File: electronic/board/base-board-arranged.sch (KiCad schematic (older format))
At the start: 96 parts, among them P1 BEAGLEBONE_BLACK, P100_0 CONN_02X10, P100_1 CONN_02X10, P100_10 CONN_02X10, P100_11 CONN_02X10, P100_12 CONN_02X10, P100_13 CONN_02X10, P100_14 CONN_02X10, P100_15 CONN_02X10, P100_16 CONN_02X10, P100_17 CONN_02X10, P100_2 CONN_02X10, P100_3 CONN_02X10, P100_4 CONN_02X10, P100_5 CONN_02X10, P100_6 CONN_02X10, P100_7 CONN_02X10, P100_8 CONN_02X10, P100_9 CONN_02X10, P2 I2C, P3 PWR, P5 CONN_02X10, P6 CONN_02X10

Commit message: Some hw, +others
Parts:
- added Q1: IRF540N, TO-220, symbol IRF540N
- added R2: 1k, Resistors_ThroughHole:Resistor_Ceramic_Horizontal_L50mm-W14mm-H13mm-p60mm, symbol R
- R100_16: footprint w_pth_resistors:R25x8 -> Resistors_ThroughHole:Resistor_Ceramic_Horizontal_L50mm-W14mm-H13mm-p60mm
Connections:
- net GND: no longer P1.A1 (GND), P1.A2 (P2), P1.B1 (GND), P1.B2 (P2), P3.2 (P2), P5.1 (P1), P5.2 (P2), P6.1 (P1), P6.2 (P2)
- net GND3: now also Q1.3 (S); no longer B4.2
- net SYS_RESETn: now also R2.2
- new net: B4.2, Q1.2 (D)
- new net: P5.1 (P1), P5.2 (P2)
- new net: Q1.1 (G), R2.1
- new net GND1: P1.B1 (GND), P1.B2 (P2), P3.2 (P2), P6.1 (P1), P6.2 (P2)
- new net GND2: P1.A1 (GND), P1.A2 (P2)
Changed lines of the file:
@@
 EESchema Schematic File Version 2
+LIBS:beagleboard
 LIBS:power
 LIBS:device
@@
 LIBS:contrib
 LIBS:valves
+LIBS:base-board-arranged-cache
 EELAYER 25 0
 EELAYER END
@@
 GPIO2_11
 Text Label 1100 8650 2    60   ~ 0
-GND
+GND2
 Text Label 1900 8650 0    60   ~ 0
-GND
+GND2
 Text Label 3300 8650 2    60   ~ 0
-GND
+GND1
 Text Label 4100 8650 0    60   ~ 0
-GND
+GND1
 Text Label 3300 8750 2    60   ~ 0
 DC_3.3Ve
@@
 	1    0    0    -1
 $EndComp
-Text Label 14450 2900 0    60   ~ 0
+Text Label 14450 4125 3    60   ~ 0
 GND3
 $Comp
@@
 Text Label 1150 5150 2    60   ~ 0
 12V+
-Text Label 1150 4850 2    60   ~ 0
-GND
 Text Label 1150 4950 2    60   ~ 0
 DC_3.3V
@@
 GND
 Text Label 2300 4850 2    60   ~ 0
-GND
+GND1
 Wire Wire Line
 	1150 4850 1650 4850
@@
 F 0 "R100_16" V 2230 5750 50  0000 C CNN
 F 1 "1K" V 2150 5750 50  0000 C CNN
-F 2 "w_pth_resistors:R25x8" V 2080 5750 30  0000 C CNN
+F 2 "Resistors_ThroughHole:Resistor_Ceramic_Horizontal_L50mm-W14mm-H13mm-p60mm" V 2080 5750 30  0000 C CNN
 F 3 "" H 2150 5750 30  0000 C CNN
 	1    2150 5750
@@
 $EndComp
 Text Label 2100 4425 2    60   ~ 0
-GND
+GND1
 Text Label 1550 4325 2    60   ~ 0
 PWR_BUT
@@
 Wire Wire Line
 	1850 4325 2100 4325
+$Comp
+L IRF540N Q1
+U 1 1 57B8B01B
+P 14350 3925
+F 0 "Q1" H 14650 4000 50  0000 L CNN
+F 1 "IRF540N" H 14600 3925 50  0000 L CNN
+F 2 "TO-220" H 14600 3850 50  0000 L CIN
+F 3 "" H 14350 3925 50  0000 L CNN
+	1    14350 3925
+	1    0    0    -1
+$EndComp
+$Comp
+L R R2
+U 1 1 57B8F1D2
+P 13850 3975
+F 0 "R2" V 13930 3975 50  0000 C CNN
+F 1 "1k" V 13850 3975 50  0000 C CNN
+F 2 "Resistors_ThroughHole:Resistor_Ceramic_Horizontal_L50mm-W14mm-H13mm-p60mm" V 13780 3975 30  0000 C CNN
+F 3 "" H 13850 3975 30  0000 C CNN
+	1    13850 3975
+	0    1    1    0
+$EndComp
+Text Label 13700 3975 2    60   ~ 0
+SYS_RESETn
+Wire Wire Line
+	14450 3725 14450 2900
+Wire Wire Line
+	14000 3975 14150 3975
 $EndSCHEMATC

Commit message: Main Board
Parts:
- removed R103_15: 1K, w_pth_resistors:RC03, symbol R
- added R3: 47k, w_pth_resistors:RC03, symbol R
- B3, B4: footprint w_pth_resistors:RC05 -> w_pth_resistors:RC07
- Q1: footprint TO-220 -> Transistors_TO-220:TO-220_Neutral123_Horizontal_LargePads
- R100_10, R100_11, R100_12, R100_13, R100_15, R100_4, R100_5, R100_6, R100_7, R100_9, R101_10, R101_11, R101_12, R101_15, R101_4, R101_5, R101_6, R101_7, R101_9, R102_10, R102_11, R102_12, R102_4, R102_5, R102_6, R102_7, R102_9, R103_10, R103_11, R103_12, R103_4, R103_5, R103_6, R103_7, R103_9: footprint w_pth_resistors:RC03 -> w_pth_resistors:RC07
- R100_16: footprint Resistors_ThroughHole:Resistor_Ceramic_Horizontal_L50mm-W14mm-H13mm-p60mm -> w_pth_resistors:R25x8
- R100_3, R101_3, R102_3: footprint w_pth_resistors:RC03 -> w_pth_resistors:RC05
- R2: value 1k -> 10k; footprint Resistors_ThroughHole:Resistor_Ceramic_Horizontal_L50mm-W14mm-H13mm-p60mm -> w_pth_resistors:RC07
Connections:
- net GND3: now also R3.1
- net GPIO3_15: now also R2.2
- net SYS_RESETn: no longer R2.2
- net at Q1.1 (G), R2.1: now also R3.2

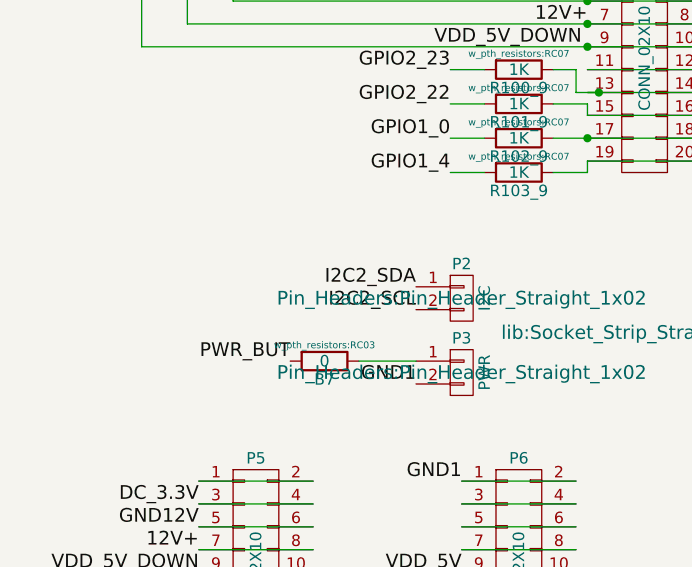
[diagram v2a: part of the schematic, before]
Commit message: Main board, IOs gated
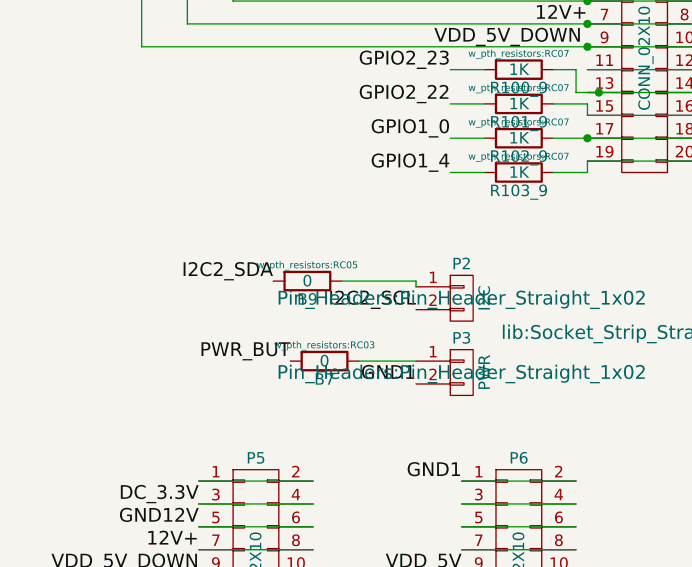
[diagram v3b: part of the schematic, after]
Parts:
- added B9: 0, w_pth_resistors:RC05, symbol R
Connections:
- net I2C2_SDA: now also B9.2; no longer P2.1 (P1)
- new net: B9.1, P2.1 (P1)
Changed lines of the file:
@@
 Text Label 2100 4100 2    60   ~ 0
 I2C2_SCL
-Text Label 2100 4000 2    60   ~ 0
+Text Label 1475 3975 2    60   ~ 0
 I2C2_SDA
 Text Label 13700 2650 2    60   ~ 0
@@
 	1    0    0    -1
 $EndComp
+$Comp
+L R B9
+U 1 1 57BF6C95
+P 1625 3975
+F 0 "B9" V 1705 3975 50  0000 C CNN
+F 1 "0" V 1625 3975 50  0000 C CNN
+F 2 "w_pth_resistors:RC05" V 1555 3975 30  0000 C CNN
+F 3 "" H 1625 3975 30  0000 C CNN
+	1    1625 3975
+	0    1    1    0
+$EndComp
+Wire Wire Line
+	1775 3975 2100 3975
+Wire Wire Line
+	2100 3975 2100 4000
 $EndSCHEMATC
